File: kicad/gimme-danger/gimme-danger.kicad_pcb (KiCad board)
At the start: 4 copper layers, 48 x 42 mm, 94 parts, among them J3 Screw_Terminal_01x06, Q1 AO3400A, Q2 AO3400A, Q3 AO3400A, Q4 AO3400A, U1 ESP32-S3-WROOM-1, U11 DDTC143EUA, U2 TYPE-C-31-M-12, U3 TPD4E1U06DCKR, U4 DC-84, U5 SKRKAEE020, U7 SKRKAEE020, U8 TPS54302, U9 INA219AIDR

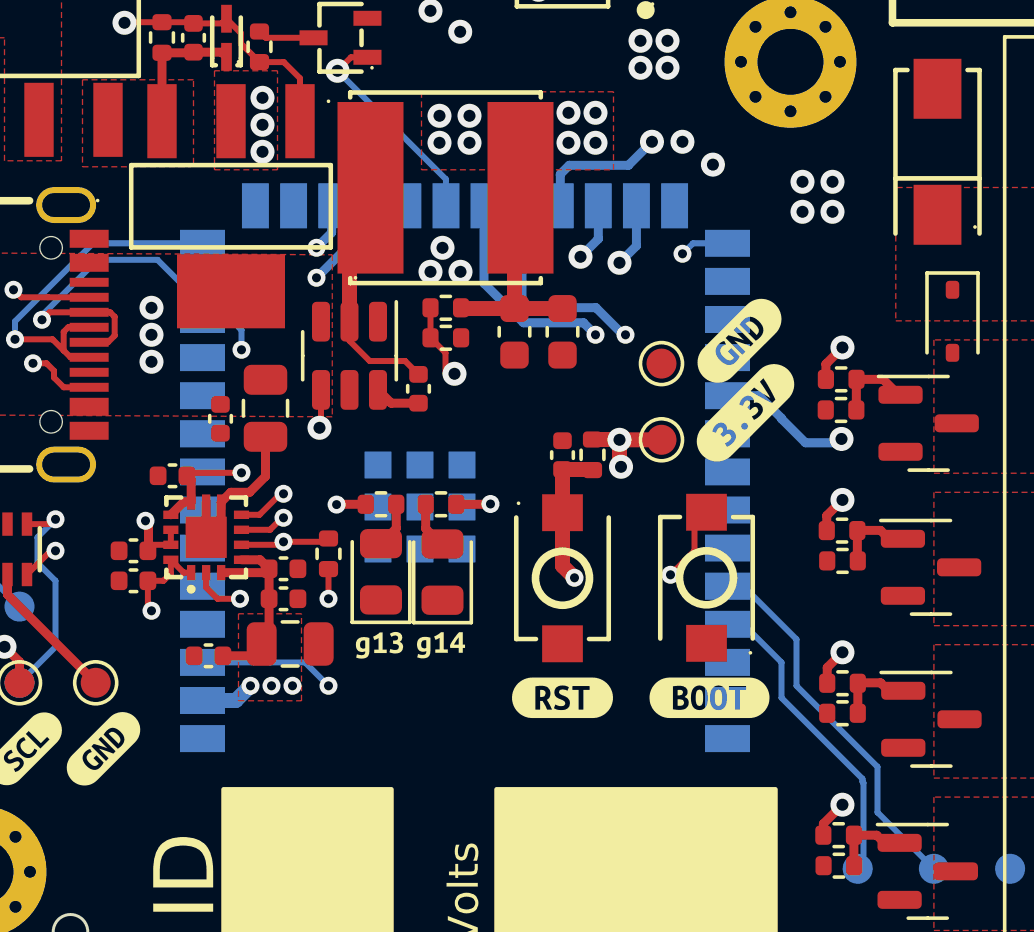
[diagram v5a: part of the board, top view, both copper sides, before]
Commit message: Changed PWM drivers gate resistor to 330
Minor routing changes
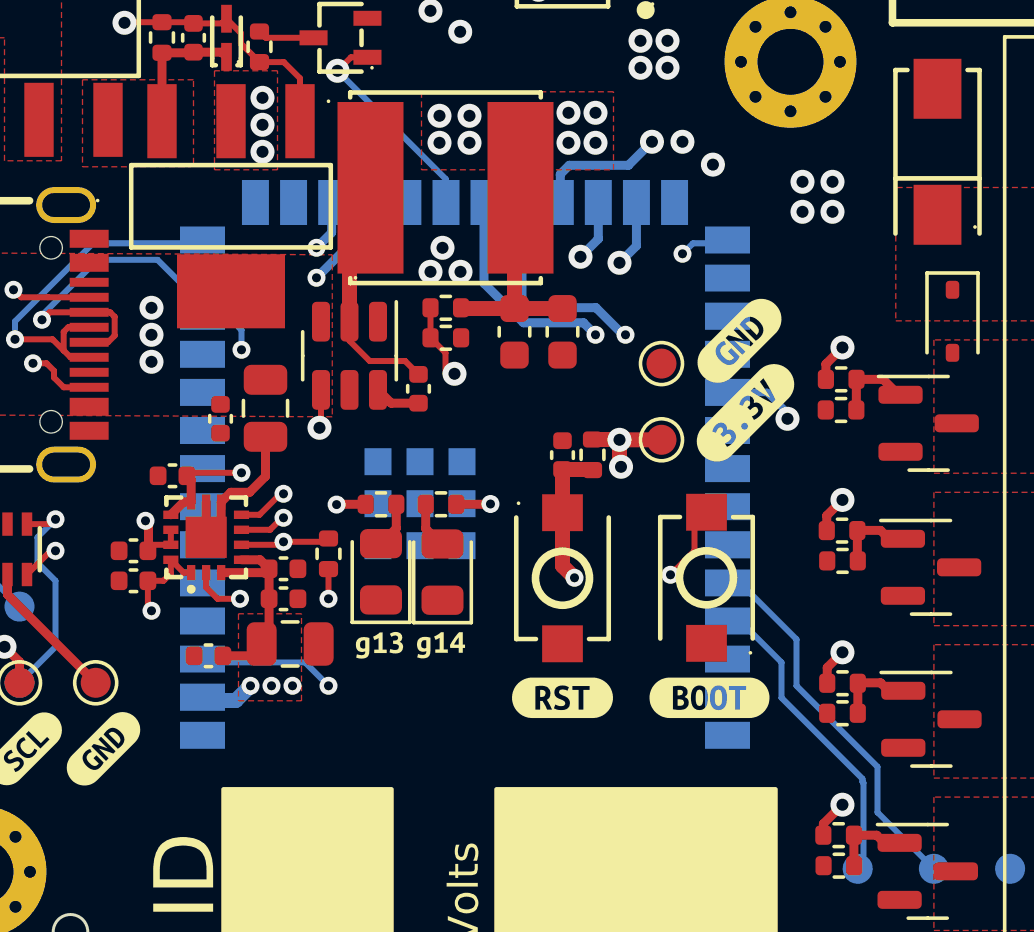
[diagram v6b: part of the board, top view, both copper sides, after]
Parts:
- R10, R19, R20, R9: value 100 -> 330
- moved U1 0.11 mm to (78.3, 117.1)

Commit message: v0.0.2a fabrication
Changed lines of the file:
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@@
     (property "Sheetfile" "gimme-danger.kicad_sch")
     (property "Sheetname" "")
+    (property "dnp" "")
+    (property "exclude_from_bom" "")
     (property "ki_description" "Mounting Hole with connection")
     (property "ki_keywords" "mounting hole")
     (zone_connect 2)
-    (attr exclude_from_pos_files)
+    (attr exclude_from_pos_files exclude_from_bom)
     (fp_text reference "H1" (at 0 -3.2) (layer "F.SilkS") hide
         (effects (font (size 1 1) (thickness 0.15)))
@@
       (net 25 "GND") (pinfunction "GND") (pintype "power_in") (zone_connect 2))
     (pad "2" smd roundrect (at -1.1375 0 270) (size 1.325 0.6) (layers "F.Cu" "F.Paste" "F.Mask") (roundrect_rratio 0.25)
-      (net 49 "Net-(U8-SW)") (pinfunction "SW") (pintype "power_out"))
+      (net 49 "Net-(U8-SW)") (pinfunction "SW") (pintype "power_out") (zone_connect 2))
     (pad "3" smd roundrect (at -1.1375 0.95 270) (size 1.325 0.6) (layers "F.Cu" "F.Paste" "F.Mask") (roundrect_rratio 0.25)
       (net 27 "VBUS") (pinfunction "VIN") (pintype "power_in") (zone_connect 2))
@@
     (property "Sheetfile" "gimme-danger.kicad_sch")
     (property "Sheetname" "")
+    (property "dnp" "")
+    (property "exclude_from_bom" "")
     (property "ki_description" "Mounting Hole with connection")
     (property "ki_keywords" "mounting hole")
     (zone_connect 2)
-    (attr exclude_from_pos_files)
+    (attr exclude_from_pos_files exclude_from_bom)
     (fp_text reference "H2" (at 0 -3.2) (layer "F.SilkS") hide
         (effects (font (size 1 1) (thickness 0.15)))
@@
     (property "Sheetfile" "gimme-danger.kicad_sch")
     (property "Sheetname" "")
+    (property "dnp" "")
+    (property "exclude_from_bom" "")
     (property "ki_description" "Mounting Hole with connection")
     (property "ki_keywords" "mounting hole")
     (zone_connect 2)
-    (attr exclude_from_pos_files)
+    (attr exclude_from_pos_files exclude_from_bom)
     (fp_text reference "H3" (at 0 -3.2) (layer "F.SilkS") hide
         (effects (font (size 1 1) (thickness 0.15)))
@@
     (property "Sheetfile" "gimme-danger.kicad_sch")
     (property "Sheetname" "")
+    (property "dnp" "")
+    (property "exclude_from_bom" "")
     (property "ki_keywords" "C718040")
     (zone_connect 2)
-    (attr through_hole)
+    (attr through_hole exclude_from_bom)
     (fp_text reference "U4" (at -2.25 -5.751054 90) (layer "F.SilkS") hide
         (effects (font (size 1 1) (thickness 0.15)))
@@
   (segment (start 75.1 107.1) (end 74.5 107.7) (width 0.5) (layer "F.Cu") (net 49))
   (segment (start 76.355 112.875) (end 75.175 112.875) (width 0.2) (layer "F.Cu") (net 49))
-  (segment (start 74.5 112.2) (end 74.5 111.5625) (width 0.2) (layer "F.Cu") (net 49))
+  (segment (start 74.5 112.2) (end 74.5 111.5625) (width 0.9) (layer "F.Cu") (net 49))
   (segment (start 75.175 112.875) (end 74.5 112.2) (width 0.2) (layer "F.Cu") (net 49))
-  (segment (start 74.5 107.7) (end 74.5 111.5625) (width 0.5) (layer "F.Cu") (net 49))
+  (segment (start 74.5 107.7) (end 74.5 111.5625) (width 0.9) (layer "F.Cu") (net 49))
   (segment (start 76.8 113.32) (end 76.355 112.875) (width 0.2) (layer "F.Cu") (net 49))
   (segment (start 75.9 107.1) (end 74.5 108.5) (width 0.5) (layer "F.Cu") (net 49))

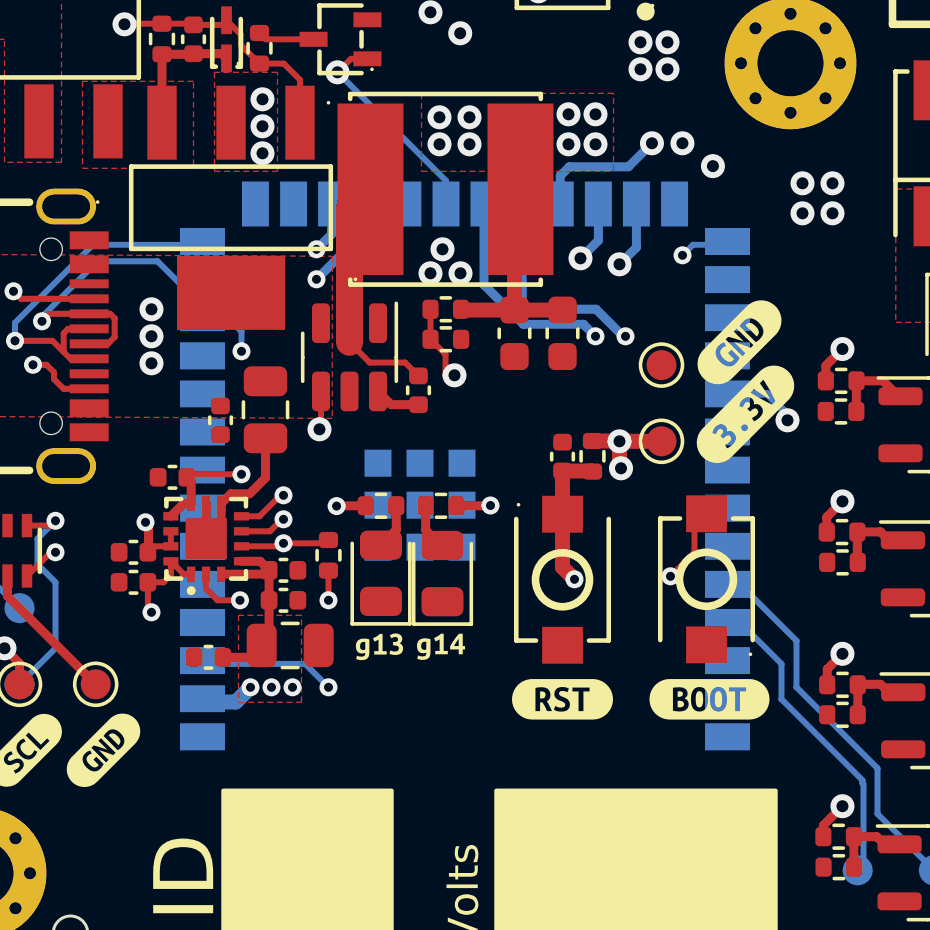
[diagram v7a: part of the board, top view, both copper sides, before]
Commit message: Updated to KiCad 8
Also updated ESP32-S3 footprint/model
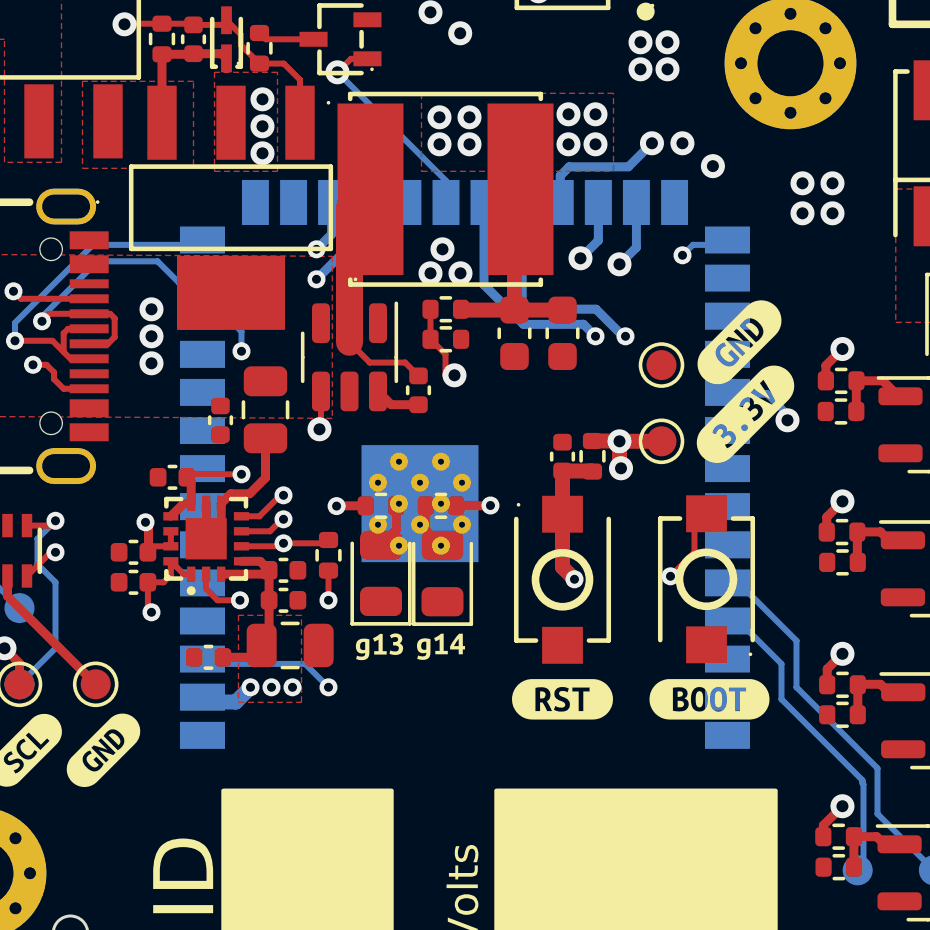
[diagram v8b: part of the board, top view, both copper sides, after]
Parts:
- U1: footprint PCM_Espressif:ESP32-S3-WROOM-1 -> RF_Module:ESP32-S3-WROOM-1
- moved U1 2.95 mm to (78.3, 120.0)
